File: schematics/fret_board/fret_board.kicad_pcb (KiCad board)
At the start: 2 copper layers, 147 x 30 mm, 6 parts, among them J1 Conn_01x06, SW1 Green, SW2 Red, SW3 Yellow, SW4 Blue, SW5 Orange

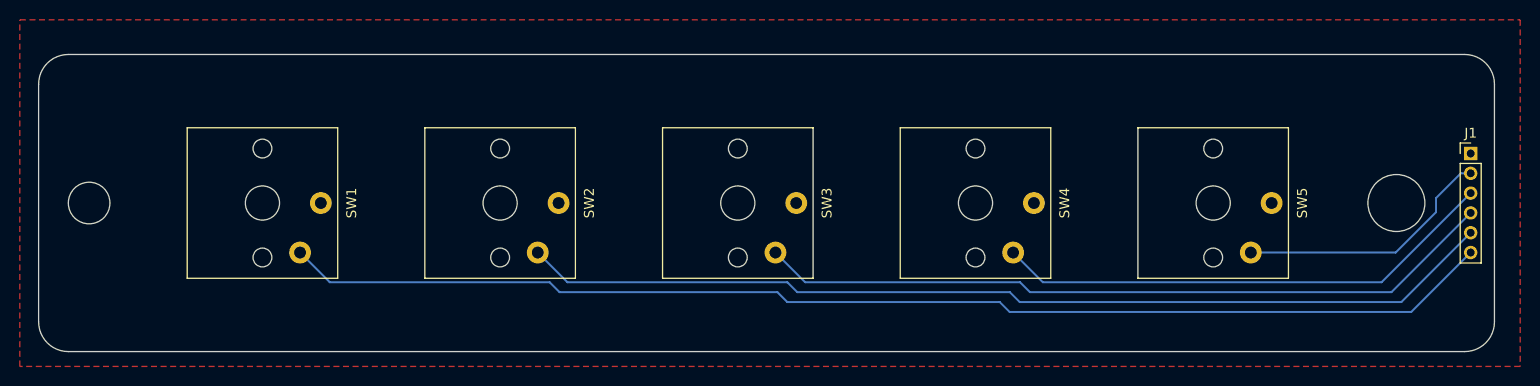
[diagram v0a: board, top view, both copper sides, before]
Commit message: Use sunken choc V1 footprint for fretboard
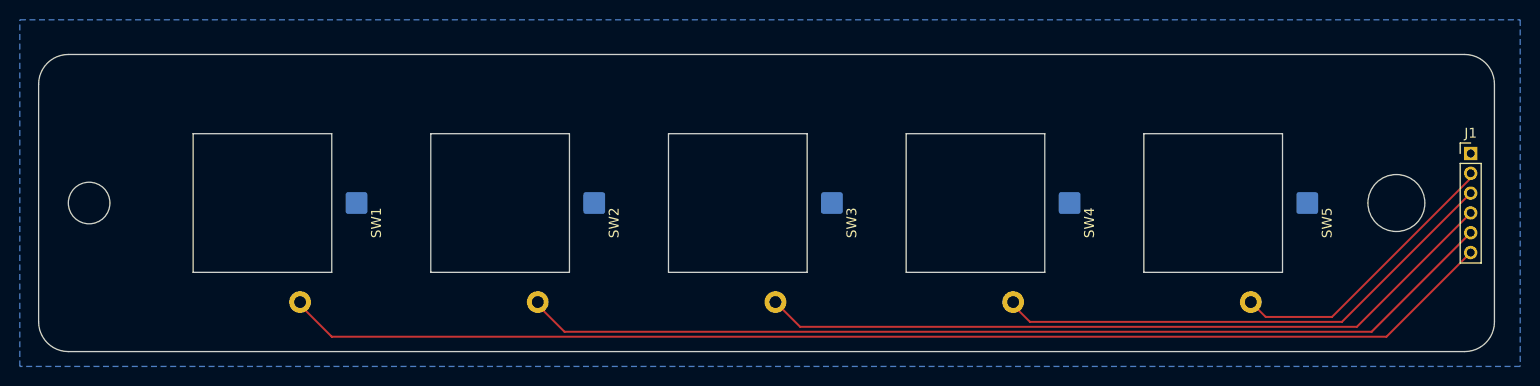
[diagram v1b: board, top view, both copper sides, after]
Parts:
- SW1, SW2, SW3, SW4, SW5: footprint ScottoKeebs_Choc:Choc_V1 -> custom_footprints:Choc_V1_sunken
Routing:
- net Net-(J1-Pin_2): track 26.3 -> 29.1 mm
- net Net-(J1-Pin_3): track 51.2 -> 52.6 mm
- net Net-(J1-Pin_4): track 75.2 -> 76.0 mm
- net Net-(J1-Pin_5): track 99.2 -> 99.8 mm
- added copper zone on B.Cu, net GND
- removed copper zone on F.Cu, net GND

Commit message: Move sunken choc pads closer
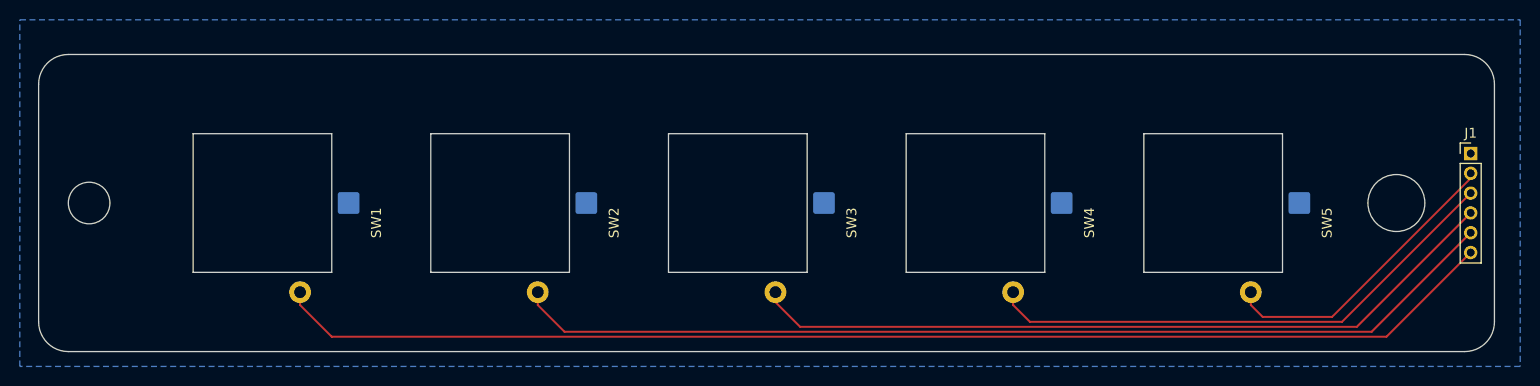
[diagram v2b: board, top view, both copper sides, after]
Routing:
- net Net-(J1-Pin_2): track 29.1 -> 30.3 mm
- net Net-(J1-Pin_6): track 123.3 -> 124.3 mm
- net Net-(J1-Pin_5): track 99.8 -> 100.8 mm
- net Net-(J1-Pin_4): track 76.0 -> 77.0 mm
- net Net-(J1-Pin_3): track 52.6 -> 53.6 mm

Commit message: Update fret_board, motherboard and strum_bar schematics
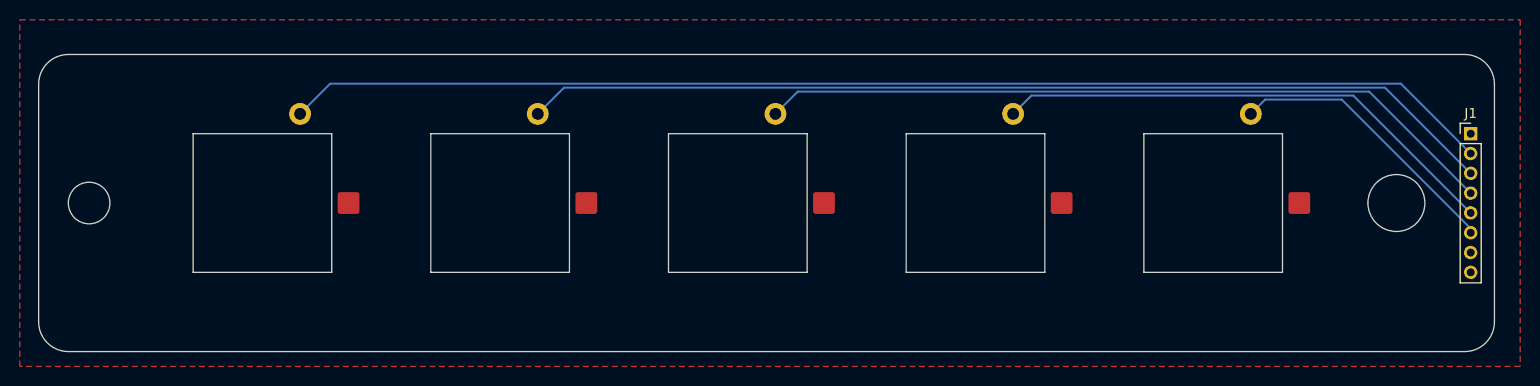
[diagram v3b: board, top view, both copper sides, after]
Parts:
- J1: value Conn_01x06 -> Conn_01x08; footprint Connector_PinHeader_2.00mm:PinHeader_1x06_P2.00mm_Vertical -> Connector_PinHeader_2.00mm:PinHeader_1x08_P2.00mm_Vertical
- SW1, SW2, SW3, SW4, SW5: moved to B.Cu
- moved J1 2.00 mm to (225.5, 92.5)
- turned SW1 to 90 degrees
- turned SW2 to 90 degrees
- turned SW3 to 90 degrees
- turned SW4 to 90 degrees
- turned SW5 to 90 degrees
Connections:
- SW1 pad 2: Net-(J1-Pin_6) -> Net-(J1-Pin_2)
- SW2 pad 2: Net-(J1-Pin_5) -> Net-(J1-Pin_3)
- SW4 pad 2: Net-(J1-Pin_3) -> Net-(J1-Pin_5)
- SW5 pad 2: Net-(J1-Pin_2) -> Net-(J1-Pin_6)
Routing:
- net Net-(J1-Pin_6): track 124.3 -> 28.6 mm
- net Net-(J1-Pin_2): track 30.3 -> 122.4 mm
- net Net-(J1-Pin_5): track 100.8 -> 51.9 mm
- net Net-(J1-Pin_3): track 53.6 -> 98.9 mm
- net Net-(J1-Pin_4): track 77.0 -> 75.4 mm
- added copper zone on F.Cu, net GND
- removed copper zone on B.Cu, net GND

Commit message: Add silkscreen graphics to each schematic
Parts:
- added G***: LOGO, LOGO, F.Cu at (215.6, 106.7)
